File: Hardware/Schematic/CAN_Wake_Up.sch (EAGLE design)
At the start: 28 parts, among them IC1 STM32F10XCXT6, IC4 LM1117MP-5.0, IC5 LM1117MP-3.3, Q1 8MHz

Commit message: Added .gitignore for schematic subdir to exclude temp. Eagle files. Updated BOM. Added Eagle BOM textfile. Updated schematic. Added Debug interface.
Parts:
- added DEBUG: (no value), pinhead:PINHD-1X4
- added R6, R7: 10k, rcl:R-EU_R0805
- C13, C14: value 20pF -> 22pF
- R2: value 10k -> 68
- R3: value 10k -> 56
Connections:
- new net DBG_SWCLK: DEBUG.3, IC1PORTA_H.PA14, R7.1
- new net DBG_SWDIO: DEBUG.2, IC1PORTA_H.PA13, R6.2
- net KL31: now also DEBUG.4, R2.1, R3.1, R7.2
- net VCC_3V3: now also DEBUG.1, R6.1
- net VCC_5V: no longer R2.1, R3.1
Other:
- moved on the sheet: C12, CAN, DA1, LED1, LED2, R2, R3, R5, SWITCH

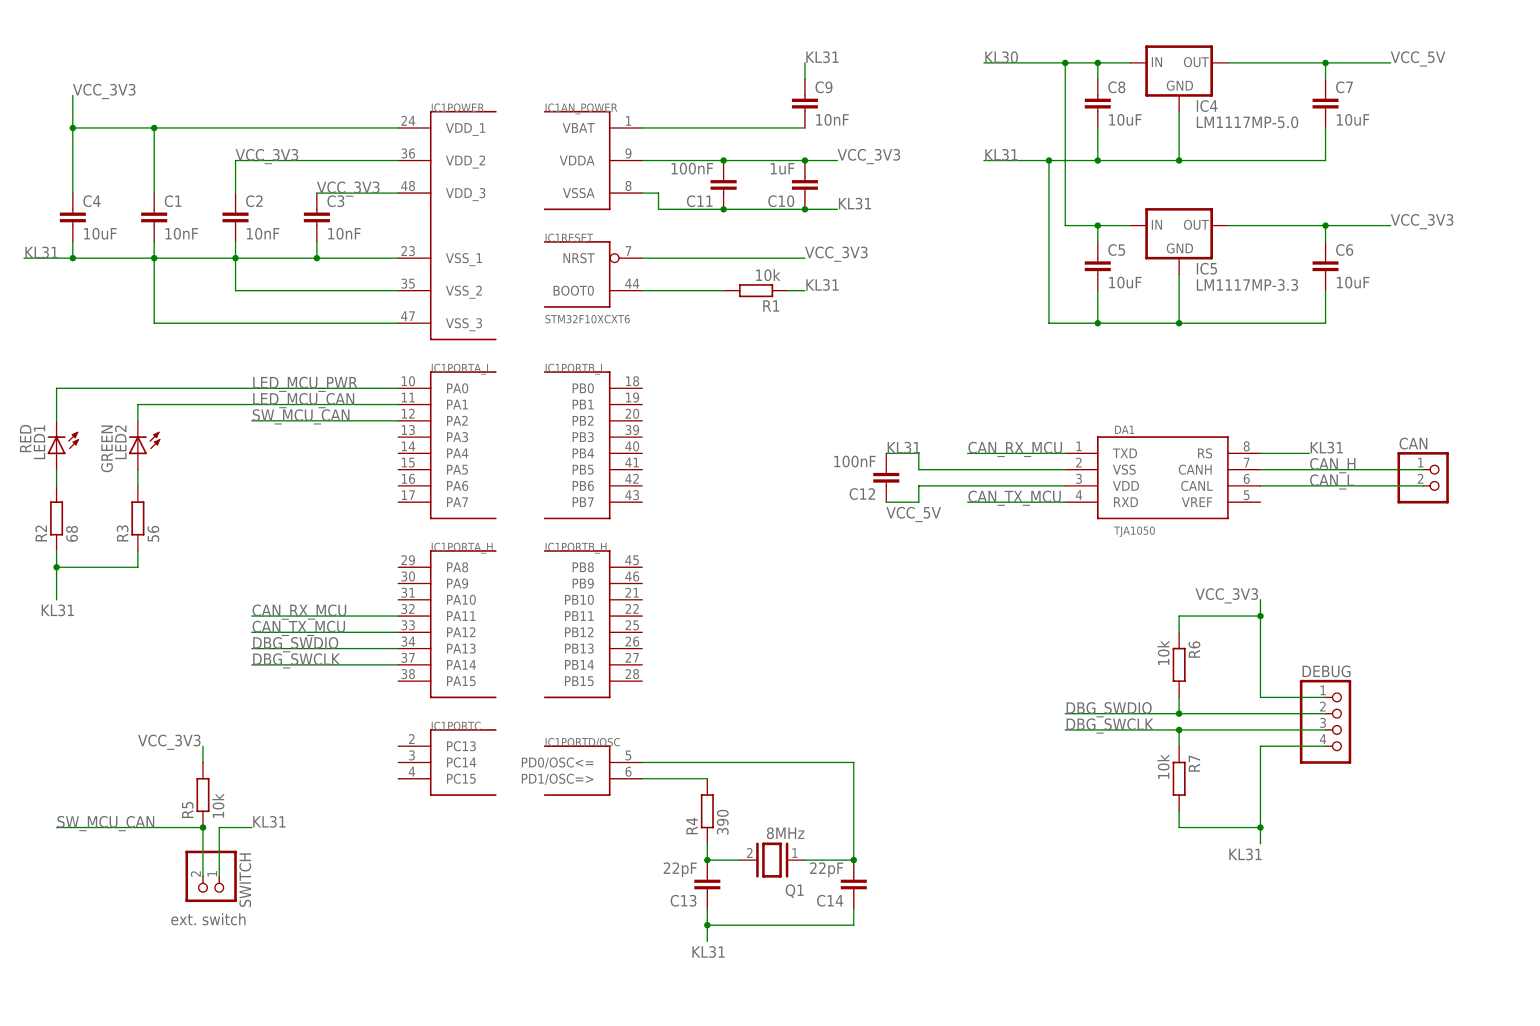
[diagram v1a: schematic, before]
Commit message: Reworked schematic. Added GND signal.
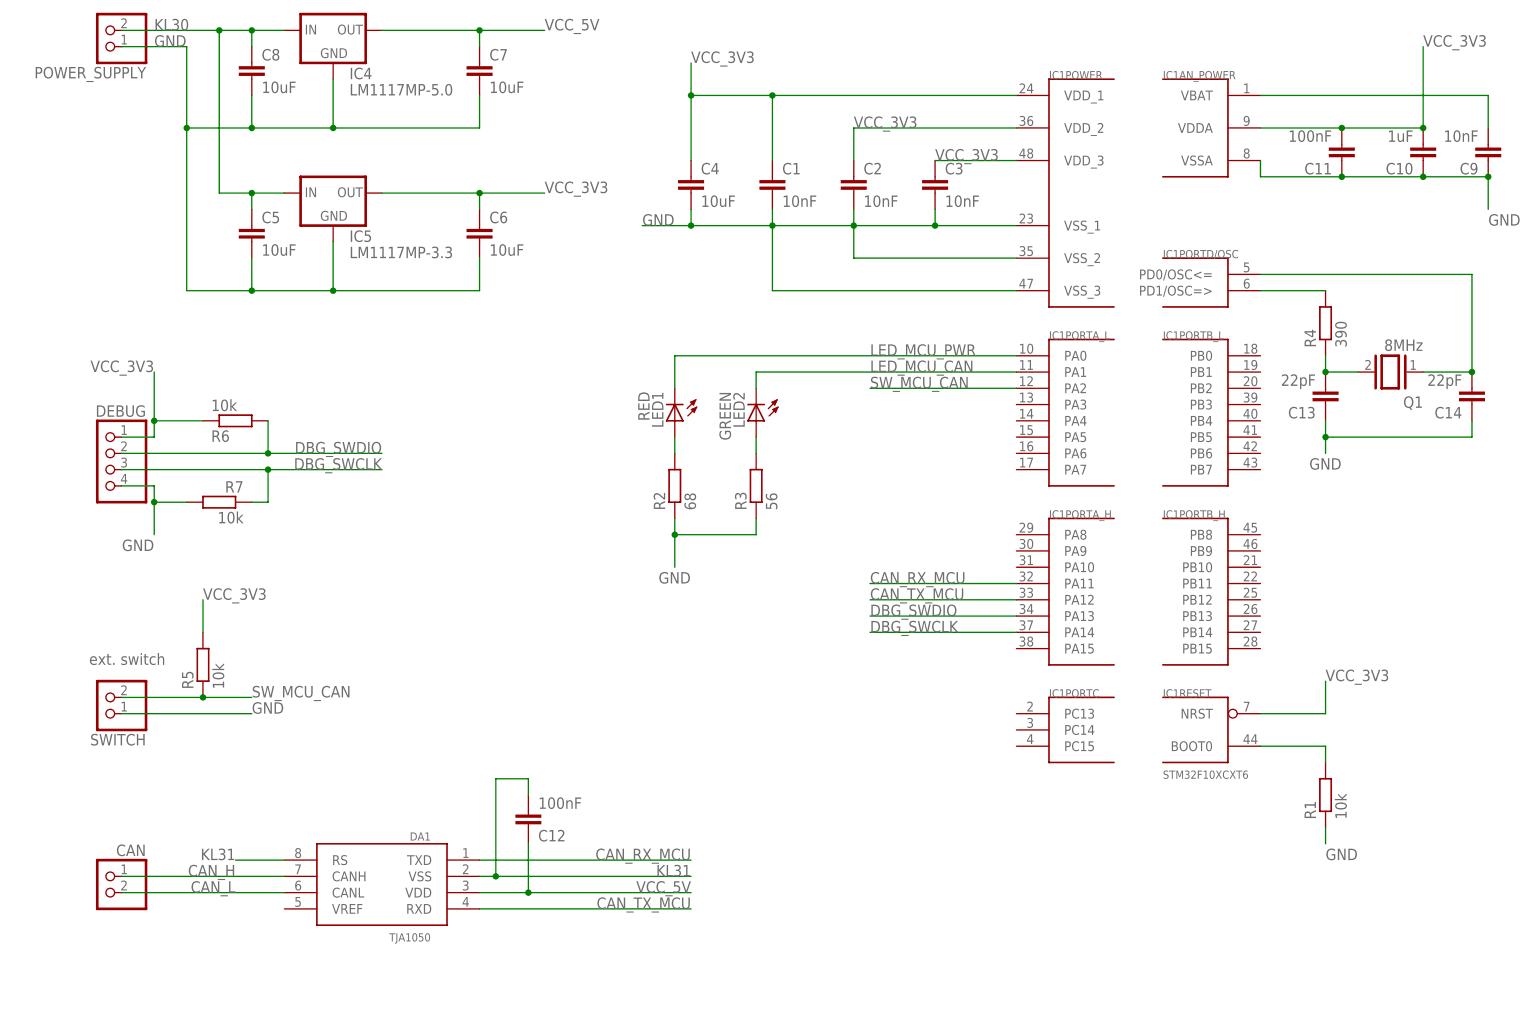
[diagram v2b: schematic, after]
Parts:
- added POWER_SUPPLY: (no value), pinhead:PINHD-1X2
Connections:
- new net GND: C1.2, C10.1, C11.1, C13.1, C14.1, C2.2, C3.2, C4.2, C5.2, C6.2, C7.2, C8.2, C9.1, DEBUG.4, IC1AN_POWER.VSSA, IC1POWER.VSS_1, IC1POWER.VSS_2, IC1POWER.VSS_3, IC4.GND, IC5.GND, POWER_SUPPLY.1, R1.1, R2.1, R3.1, R7.2, SWITCH.1
- net KL30: now also POWER_SUPPLY.2
- net KL31: no longer C1.2, C10.1, C11.1, C13.1, C14.1, C2.2, C3.2, C4.2, C5.2, C6.2, C7.2, C8.2, C9.1, DEBUG.4, IC1AN_POWER.VSSA, IC1POWER.VSS_1, IC1POWER.VSS_2, IC1POWER.VSS_3, IC4.GND, IC5.GND, R1.1, R2.1, R3.1, R7.2, SWITCH.1
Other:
- moved on the sheet: C1, C10, C11, C12, C13, C14, C2, C3, C4, C5, C6, C7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
